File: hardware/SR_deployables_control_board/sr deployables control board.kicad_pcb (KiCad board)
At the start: 2 copper layers, 34.2 x 35 mm, 26 parts, among them J1 Conn_01x12_Pin, J2 Conn_01x02_Pin, J3 Conn_01x07_Pin, Q3 2N7002, Q4 2N7002, U1 MCP3002, U2 DRV8833PW

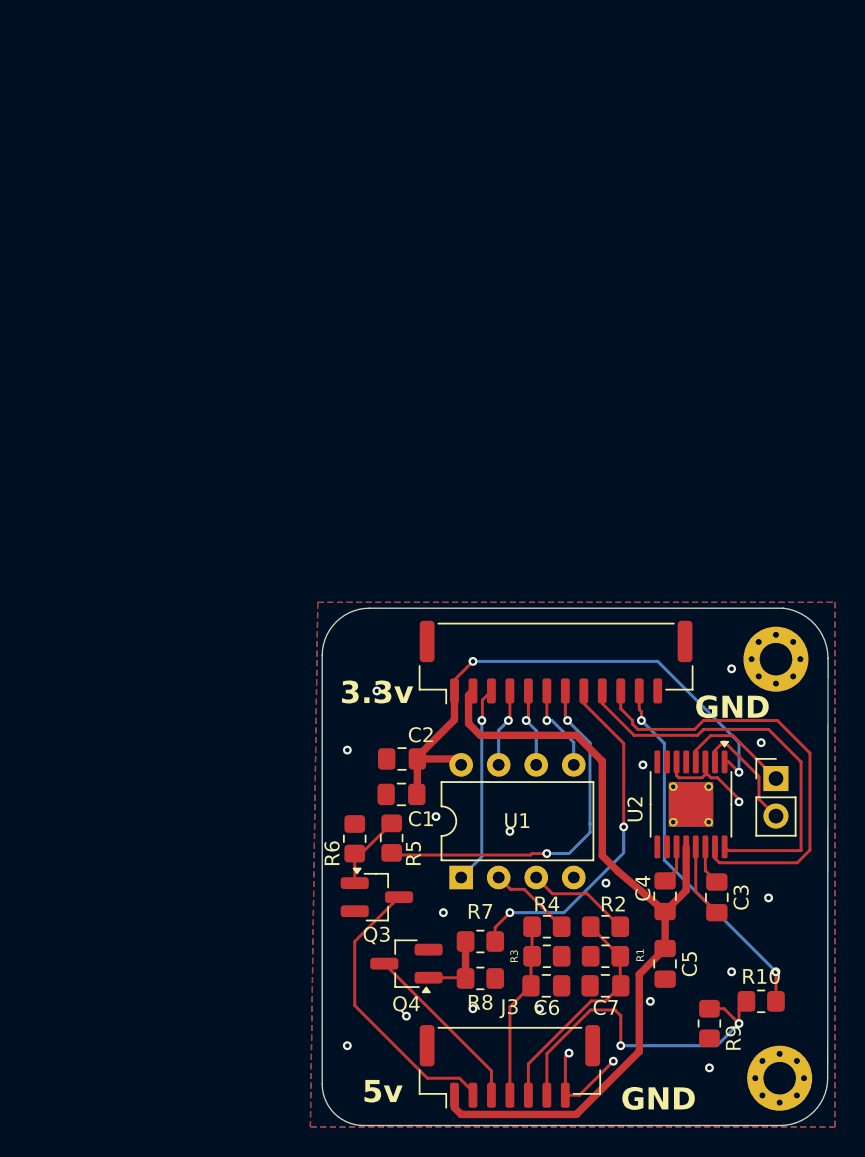
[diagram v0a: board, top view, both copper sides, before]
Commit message: feat: New motor driver/pi interface pcb for kibisis & space resources
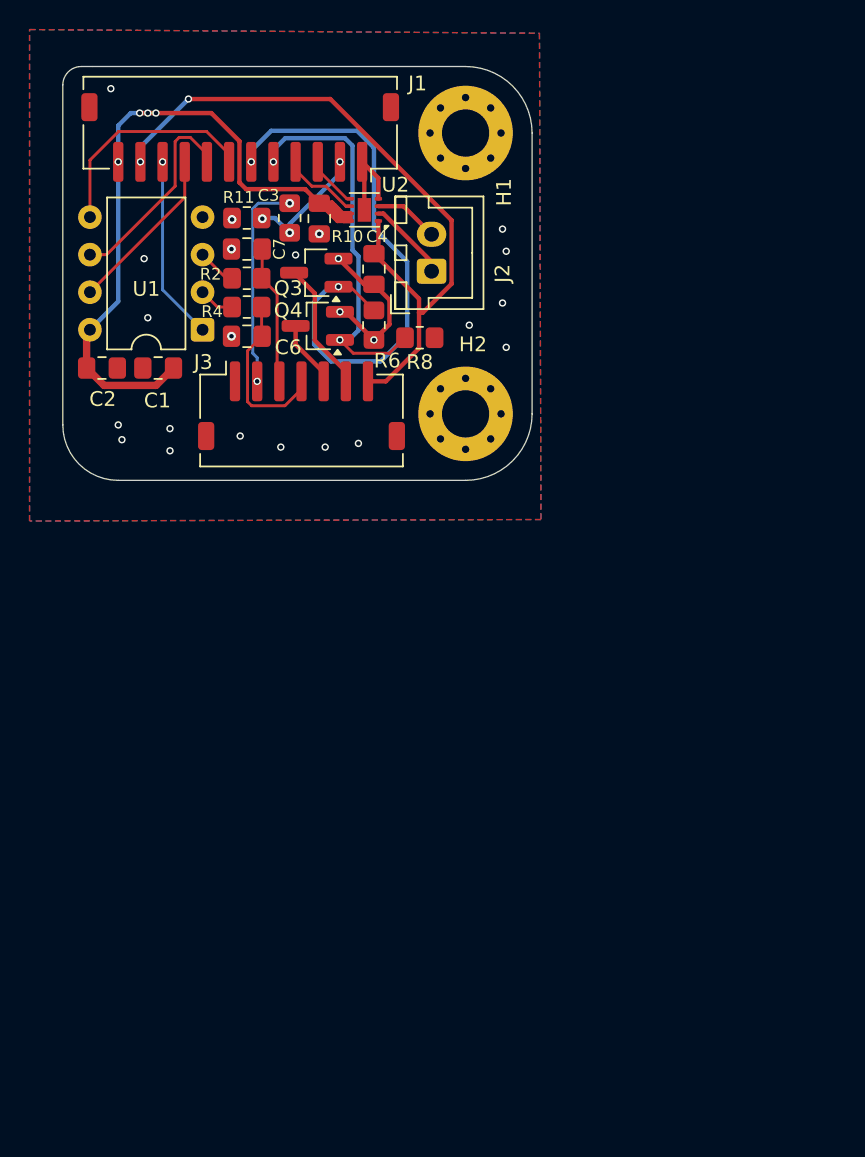
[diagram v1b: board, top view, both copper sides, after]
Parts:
- removed C5: 10uF, Capacitor_SMD:C_0805_2012Metric_Pad1.18x1.45mm_HandSolder
- removed R1, R3, R9: 10k, Resistor_SMD:R_0805_2012Metric_Pad1.20x1.40mm_HandSolder
- removed R5, R7: 100, Resistor_SMD:R_0805_2012Metric_Pad1.20x1.40mm_HandSolder
- added R11: 18k, Resistor_SMD:R_0805_2012Metric_Pad1.20x1.40mm_HandSolder, F.Cu at (103.7, 46.0)
- C3: value 2.2uF 6.3v -> 100nF
- C4: value 0.01uF, 16v ceramic X7R -> 100nF
- H1, H2: footprint MountingHole:MountingHole_2.2mm_M2_Pad_Via -> MountingHole:MountingHole_3.2mm_M3_Pad_Via
- J1: footprint Connector_JST:JST_GH_BM12B-GHS-TBT_1x12-1MP_P1.25mm_Vertical -> Connector_JST:JST_ZH_S12B-ZR-SM4A-TF_1x12-1MP_P1.50mm_Horizontal
- J2: value Conn_01x02_Pin -> MOTOR_CONN; footprint Connector_PinHeader_2.54mm:PinHeader_1x02_P2.54mm_Vertical -> Connector_JST:JST_XH_B2B-XH-A_1x02_P2.50mm_Vertical
- J3: footprint Connector_JST:JST_GH_BM07B-GHS-TBT_1x07-1MP_P1.25mm_Vertical -> Connector_JST:JST_ZH_S7B-ZR-SM4A-TF_1x07-1MP_P1.50mm_Horizontal
- Q3: value 2N7002 -> AO3400A
- R10: value 20k -> 10k
- U2: value DRV8833PW -> DRV8837C; footprint Package_SO:TSSOP-16-1EP_4.4x5mm_P0.65mm_EP3x3mm_ThermalVias -> Package_SON:WSON-8-1EP_2x2mm_P0.5mm_EP0.9x1.6mm
- moved R10 61.9 mm to (106.6, 46.0), turned to -90 degrees
- moved C7 55.4 mm to (103.7, 48.1)
- moved C3 53.2 mm to (108.6, 46.0), turned to 90 degrees
- moved R2 50.1 mm to (103.7, 50.1), turned to 180 degrees
- moved H2 49.7 mm to (118.5, 59.2)
- moved C6 48.4 mm to (103.7, 54.0), turned to 180 degrees
- moved J3 46.9 mm to (107.4, 58.7)
- moved C4 46.8 mm to (112.3, 49.5)
- moved R4 46.6 mm to (103.7, 52.0), turned to 180 degrees
- moved U2 45.9 mm to (111.7, 45.5), turned to 180 degrees
- moved Q4 43.6 mm to (108.5, 53.3)
- moved R8 43.5 mm to (115.4, 54.1)
- moved Q3 42.4 mm to (108.4, 49.7), turned to 180 degrees
- moved J2 41.5 mm to (116.2, 49.6), turned to 90 degrees
- moved J1 41.4 mm to (103.2, 40.5), turned to 180 degrees
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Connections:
- C3 pad 1: Net-(U2-VINT) -> GND
- C3 pad 2: GND -> +3.3V
- C4 pad 1: VM -> GND
- C4 pad 2: Net-(U2-VCP) -> +5V
- J1 pad 1: +3.3V -> GND
- J1 pad 10: AIN2 -> CS
- J1 pad 11: SWITCH -> +5V
- J1 pad 12: GND -> +3.3V
- J1 pad 2: VM -> SWITCH
- J1 pad 3: CS -> AIN2
- J1 pad 4: CLK -> AIN1
- J1 pad 5: MISO -> GATE2
- J1 pad 6: MOSI -> GATE1
- J1 pad 7: GATE1 -> MOSI
- J1 pad 8: GATE2 -> MISO
- J1 pad 9: AIN1 -> CLK
- J1 pad MP: (no net) -> unconnected-(J1-MountPin-PadMP)
- J3 pad 1: VM -> GND
- J3 pad 2: DRAIN1 -> Net-(J3-Pin_2)
- J3 pad 3: DRAIN2 -> CH1
- J3 pad 5: CH1 -> DRAIN2
- J3 pad 6: Net-(J3-Pin_6) -> DRAIN1
- J3 pad 7: GND -> +5V
- J3 pad MP: (no net) -> unconnected-(J3-MountPin-PadMP)
- Q3 pad 1: Net-(Q3-G) -> GATE1
- Q4 pad 1: Net-(Q4-G) -> GATE2
- R10 pad 1: Net-(J3-Pin_6) -> Net-(J3-Pin_2)
- R6 pad 2: Net-(Q3-G) -> GATE1
- R8 pad 2: Net-(Q4-G) -> GATE2
- U2 pad 1: +3.3V -> +5V
- U2 pad 2: Net-(J2-Pin_2) -> Net-(J2-Pin_1)
- U2 pad 3: GND -> Net-(J2-Pin_2)
- U2 pad 4: Net-(J2-Pin_1) -> GND
- U2 pad 5: unconnected-(U2-BOUT2-Pad5) -> AIN2
- U2 pad 6: GND -> AIN1
- U2 pad 7: unconnected-(U2-BOUT1-Pad7) -> +3.3V
- U2 pad 8: unconnected-(U2-~{FAULT}-Pad8) -> +3.3V
- U2 pad 9: unconnected-(U2-BIN1-Pad9) -> GND
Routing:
- net VM: track 55.0 -> 0.00 mm
- net +5V: track 0.00 -> 48.6 mm, vias 0 -> 2
- net AIN2: track 30.1 -> 3.54 mm
- net Net-(J3-Pin_6): track 24.0 -> 0.00 mm, vias 2 -> 0
- net AIN1: track 27.5 -> 5.26 mm
- net +3.3V: track 37.2 -> 56.6 mm, vias 2 -> 4
- net SWITCH: track 24.8 -> 8.49 mm, vias 2 -> 3
- net Net-(J3-Pin_2): track 0.00 -> 14.5 mm, vias 0 -> 2
- net GATE1: track 24.3 -> 38.6 mm
- net DRAIN1: track 19.2 -> 8.80 mm
- net MOSI: track 5.96 -> 15.2 mm, vias 1 -> 0
- net MISO: track 5.34 -> 14.0 mm, vias 1 -> 0
- net DRAIN2: track 11.9 -> 4.54 mm
- net CLK: track 5.31 -> 11.5 mm, vias 1 -> 0
- net CH1: track 15.4 -> 9.46 mm
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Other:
- board size 34.2 x 35 mm -> 31.8 x 28 mm
- board text removed: "3.3v"
- board text removed: "5v"
- board text removed: "GND"

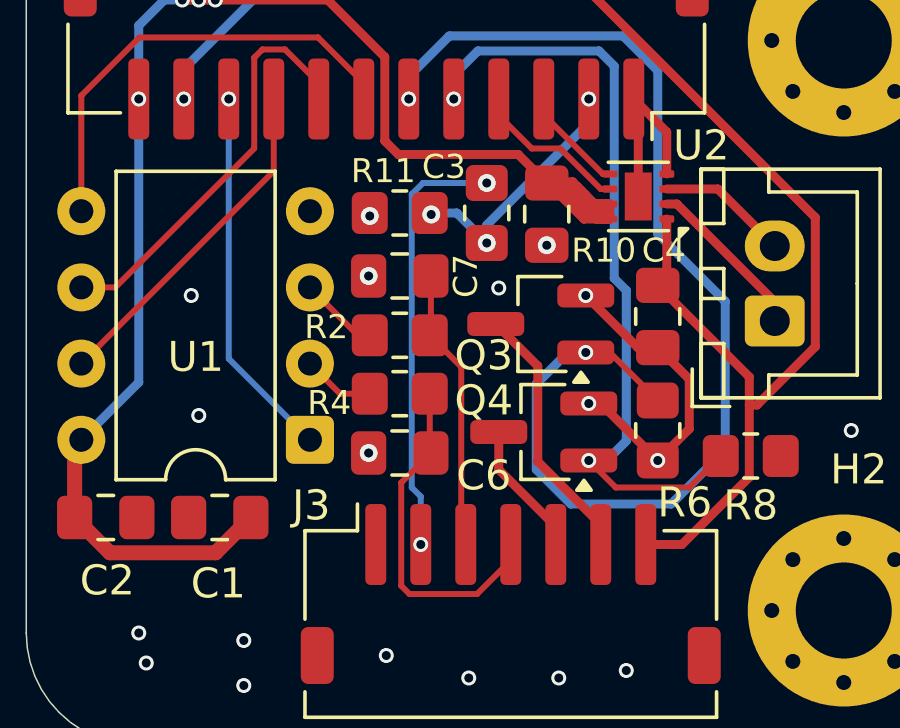
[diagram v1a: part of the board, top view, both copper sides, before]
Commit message: Retraced voltage divider
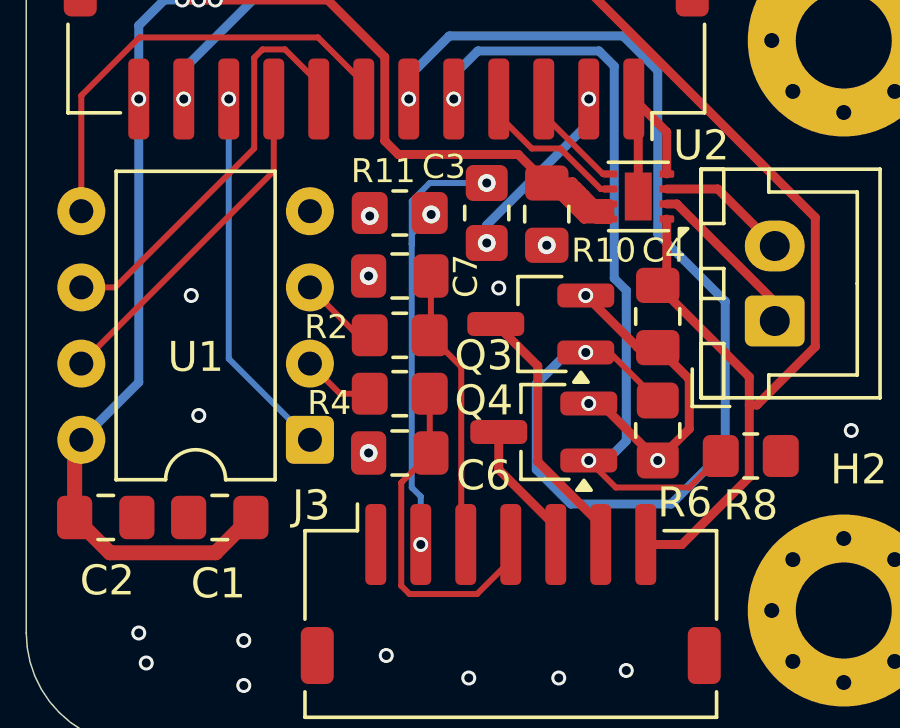
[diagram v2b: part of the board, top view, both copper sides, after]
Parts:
- R10: value 10k -> 8k
- R11: value 18k -> 10k
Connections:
- R11 pad 2: SWITCH -> Net-(J3-Pin_2)
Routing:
- net SWITCH: track 8.49 -> 6.21 mm, vias 3 -> 2
- net Net-(J3-Pin_2): track 14.5 -> 15.7 mm, vias 2 -> 3
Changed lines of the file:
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@@
 	(version 20241229)
 	(generator "pcbnew")
-	(generator_version "9.99")
+	(generator_version "9.0")
 	(general
 		(thickness 1.6)
@@
 			)
 		)
-		(property "Value" "10k"
+		(property "Value" "8k"
 			(at 0 1.65 90)
 			(layer "F.Fab")
@@
 			)
 		)
-		(property "Value" "18k"
+		(property "Value" "10k"
 			(at 0 1.65 0)
 			(layer "F.Fab")
@@
 			(layers "F.Cu" "F.Mask" "F.Paste")
 			(roundrect_rratio 0.208333)
-			(net 15 "SWITCH")
+			(net 4 "Net-(J3-Pin_2)")
 			(pintype "passive")
 		)
@@
 	)
 	(via
+		(at 104.749293 46.049293)
+		(size 0.6)
+		(drill 0.3)
+		(layers "F.Cu" "B.Cu")
+		(net 4)
+	)
+	(via
 		(at 106.6 45)
 		(size 0.6)
@@
 	)
 	(segment
-		(start 104.099 45.376028)
-		(end 104.099 55.149)
+		(start 104.099 47.05)
+		(end 104.099 46.699586)
 		(width 0.2)
 		(layer "B.Cu")
@@
 	(segment
 		(start 104.4 55.45)
-		(end 104.4 57.05)
+		(end 104.099 55.149)
 		(width 0.2)
 		(layer "B.Cu")
@@
 	)
 	(segment
-		(start 104.475028 45)
-		(end 104.099 45.376028)
+		(start 104.099 46.699586)
+		(end 104.749293 46.049293)
 		(width 0.2)
 		(layer "B.Cu")
@@
 	)
 	(segment
-		(start 106.6 45)
-		(end 104.475028 45)
+		(start 104.7 45)
+		(end 106.6 45)
 		(width 0.2)
 		(layer "B.Cu")
@@
 	)
 	(segment
-		(start 104.099 55.149)
+		(start 104.4 57.05)
 		(end 104.4 55.45)
 		(width 0.2)
@@
 		(net 4)
 	)
+	(segment
+		(start 104.099 47.05)
+		(end 104.099 45.601)
+		(width 0.2)
+		(layer "B.Cu")
+		(net 4)
+	)
+	(segment
+		(start 104.099 55.149)
+		(end 104.099 47.05)
+		(width 0.2)
+		(layer "B.Cu")
+		(net 4)
+	)
+	(segment
+		(start 104.749293 46.049293)
+		(end 104.798586 46)
+		(width 0.3)
+		(layer "B.Cu")
+		(net 4)
+	)
+	(segment
+		(start 104.099 45.601)
+		(end 104.7 45)
+		(width 0.2)
+		(layer "B.Cu")
+		(net 4)
+	)
 	(via
 		(at 98 42.2)
@@
 	)
 	(via
-		(at 104.749293 46.049293)
-		(size 0.6)
-		(drill 0.3)
-		(layers "F.Cu" "B.Cu")
-		(net 15)
-	)
-	(via
 		(at 106.6 47)
 		(size 0.6)
@@
 	)
 	(segment
-		(start 105.6 46)
-		(end 106.6 47)
-		(width 0.3)
-		(layer "B.Cu")
-		(net 15)
-	)
-	(segment
 		(start 110 43)
 		(end 106.6 46.4)
 		(width 0.3)
 		(layer "B.Cu")
-		(net 15)
-	)
-	(segment
-		(start 104.749293 46.049293)
-		(end 104.798586 46)
-		(width 0.3)
-		(layer "B.Cu")
-		(net 15)
-	)
-	(segment
-		(start 104.798586 46)
-		(end 105.6 46)
-		(width 0.3)
-		(layer "B.Cu")
